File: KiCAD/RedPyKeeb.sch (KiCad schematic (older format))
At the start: 4 parts, among them J0 Conn_01x04_MountingPin_PicoUSB, U0 USB_Pico, U1,0 Board_main_Pico, U1,1 Board_side_Pico

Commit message: Update KiCAD files
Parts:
- removed J0: Conn_01x04_MountingPin_PicoUSB, symbol Connector_Generic_MountingPin:Conn_01x04_MountingPin
- removed U1,0: Board_main_Pico, MCU_RaspberryPi_and_Boards:RPi_Pico_SMD_TH, symbol MCU_RaspberryPi_and_Boards:Pico
- removed U1,1: Board_side_Pico, MCU_RaspberryPi_and_Boards:RPi_Pico_SMD_TH, symbol MCU_RaspberryPi_and_Boards:Pico
- added J0, J1: Conn_01x04, Connector_JST:JST_EH_S4B-EH_1x04_P2.50mm_Horizontal, symbol Connector_Generic:Conn_01x04
- added U1, U2, U3: MCP23017_SO, Package_SO:SOIC-28W_7.5x17.9mm_P1.27mm, symbol Interface_Expansion:MCP23017_SO
- U0: footprint RPi_Pico:RPi_Pico_SMD_TH -> MCU_RaspberryPi_and_Boards:RPi_Pico_SMD_TH
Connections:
- net labels added: GNDPWR, IO_INT0, IO_INT1, IO_INT2, IO_INT3, LED_SCL_ROW0, LED_SCL_ROW1, LED_SCL_ROW2, LED_SCL_ROW3, LED_SCL_ROW4, LED_SCL_ROW5, LED_SCL_ROW6, LED_SDA_ROW0, LED_SDA_ROW1, LED_SDA_ROW2, LED_SDA_ROW3, LED_SDA_ROW4, LED_SDA_ROW5, LED_SDA_ROW6, MAIN_VBUS, USB_DN, USB_DP
- net labels removed: I2C_SCL1, I2C_SDA1, KEY_ROW0,1, KEY_ROW1,1, KEY_ROW2,1, KEY_ROW3,1, KEY_ROW4,1, KEY_ROW5,1, PICO_PWR
- wire segments 4 -> 0
- no-connect marks 82 -> 42
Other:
- note added: "LED IO controller"
- note added: "Use I2C for interboard comms.\nSDA0 on GPIO0\nSCL0 on GPIO1"
- note removed: "This needs a footprint that will allow me to solder a small 4 pin connector to connect to the C3 daughterboard that will screw into the case."
- note removed: "Use I2C for interboard comms.\nSDA0 on GPIO0\nSCL0 on GPIO1\nSDA1 on GPIO4\nSCL1 on GPIO5"
- moved on the sheet: U0

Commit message: Update KiCAD files
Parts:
- added C1, C2, C3: 0805B104K100CT, Capacitors_SMD:C_0805_HandSoldering, symbol Device:CP
- U0: footprint MCU_RaspberryPi_and_Boards:RPi_Pico_SMD_TH -> Custom_pico:RPi_Pico_SMD_TH; symbol MCU_RaspberryPi_and_Boards:Pico -> RPI_Pico:Pico
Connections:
- net GNDPWR: now also U0.44 (TP1), C1.2, C2.2, C3.2; no longer U0.38 (GND)
- net MAIN_VBUS: now also C1.1, C2.1, C3.1
- net USB_DN: now also U0.45 (TP2)
- net USB_DP: now also U0.46 (TP3)
- no-connect marks 42 -> 43
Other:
- note added: "0805B104K100CT for capacitors\n100nF"
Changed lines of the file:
@@
 $EndDescr
 $Sheet
-S 9650 750  500  300
+S 9150 750  500  300
 U 604A5E2C
 F0 "key_matrix" 39
@@
 Text Notes 2350 800  0    59   ~ 0
 TODO: Power bus needs to be sorted, see Unified-Daughterboard?\n
-Text Notes 11150 1350 2    59   ~ 0
+Text Notes 10650 1350 2    59   ~ 0
 KEY_* originates from this sheet
-$Comp
-L MCU_RaspberryPi_and_Boards:Pico U0
-U 1 1 62848745
-P 1900 3000
-F 0 "U0" H 1900 4215 50  0000 C CNN
-F 1 "USB_Pico" H 1900 4124 50  0000 C CNN
-F 2 "MCU_RaspberryPi_and_Boards:RPi_Pico_SMD_TH" V 1900 3000 50  0001 C CNN
-F 3 "" H 1900 3000 50  0001 C CNN
-	1    1900 3000
-	1    0    0    -1
-$EndComp
 Text GLabel 1200 2050 0    39   BiDi ~ 0
 I2C_SDA0
@@
 Text GLabel 7150 2350 2    39   BiDi ~ 0
 KEY_COL14
-Text GLabel 4200 2050 2    39   BiDi ~ 0
-MAIN_VBUS
-$Comp
-L power:GNDPWR #PWR0101
-U 1 1 633BF01D
-P 2600 2250
-F 0 "#PWR0101" H 2600 2050 50  0001 C CNN
-F 1 "GNDPWR" V 2605 2142 50  0000 R CNN
-F 2 "" H 2600 2200 50  0001 C CNN
-F 3 "" H 2600 2200 50  0001 C CNN
-	1    2600 2250
-	0    -1   -1   0
-$EndComp
+Text GLabel 3750 1800 0    39   BiDi ~ 0
+MAIN_VBUS
 $Comp
 L power:GNDPWR #PWR0102
@@
 	0    -1   -1   0
 $EndComp
-Text GLabel 6450 2050 2    39   BiDi ~ 0
-MAIN_VBUS
 Text GLabel 5750 2350 0    39   BiDi ~ 0
 I2C_SDA0
@@
 	0    -1   -1   0
 $EndComp
-Text GLabel 8800 2050 2    39   BiDi ~ 0
-MAIN_VBUS
 Text Notes 9100 1850 2    39   ~ 0
 LED IO controller
@@
 $EndComp
 $Comp
-L power:GNDPWR #PWR?
+L power:GNDPWR #PWR0101
 U 1 1 6434583E
 P 5200 1250
-F 0 "#PWR?" H 5200 1050 50  0001 C CNN
+F 0 "#PWR0101" H 5200 1050 50  0001 C CNN
 F 1 "GNDPWR" V 5205 1142 50  0000 R CNN
 F 2 "" H 5200 1200 50  0001 C CNN
@@
 $EndComp
 $Comp
-L power:GNDPWR #PWR?
+L power:GNDPWR #PWR0104
 U 1 1 64901E61
 P 3500 3950
-F 0 "#PWR?" H 3500 3750 50  0001 C CNN
+F 0 "#PWR0104" H 3500 3750 50  0001 C CNN
 F 1 "GNDPWR" V 3504 3841 50  0000 R CNN
 F 2 "" H 3500 3900 50  0001 C CNN
@@
 $EndComp
 $Comp
-L power:GNDPWR #PWR?
+L power:GNDPWR #PWR0106
 U 1 1 64903402
 P 3500 3850
-F 0 "#PWR?" H 3500 3650 50  0001 C CNN
+F 0 "#PWR0106" H 3500 3650 50  0001 C CNN
 F 1 "GNDPWR" V 3504 3741 50  0000 R CNN
 F 2 "" H 3500 3800 50  0001 C CNN
@@
 $EndComp
 $Comp
-L power:GNDPWR #PWR?
+L power:GNDPWR #PWR0107
 U 1 1 649035CF
 P 3500 3750
-F 0 "#PWR?" H 3500 3550 50  0001 C CNN
+F 0 "#PWR0107" H 3500 3550 50  0001 C CNN
 F 1 "GNDPWR" V 3504 3641 50  0000 R CNN
 F 2 "" H 3500 3700 50  0001 C CNN
@@
 $EndComp
 $Comp
-L power:GNDPWR #PWR?
+L power:GNDPWR #PWR0108
 U 1 1 649043C1
 P 5750 3850
-F 0 "#PWR?" H 5750 3650 50  0001 C CNN
+F 0 "#PWR0108" H 5750 3650 50  0001 C CNN
 F 1 "GNDPWR" V 5754 3741 50  0000 R CNN
 F 2 "" H 5750 3800 50  0001 C CNN
@@
 $EndComp
 $Comp
-L power:GNDPWR #PWR?
+L power:GNDPWR #PWR0109
 U 1 1 64904490
 P 5750 3750
-F 0 "#PWR?" H 5750 3550 50  0001 C CNN
+F 0 "#PWR0109" H 5750 3550 50  0001 C CNN
 F 1 "GNDPWR" V 5754 3641 50  0000 R CNN
 F 2 "" H 5750 3700 50  0001 C CNN
@@
 $EndComp
 $Comp
-L power:GNDPWR #PWR?
+L power:GNDPWR #PWR0110
 U 1 1 64904A18
 P 8100 3750
-F 0 "#PWR?" H 8100 3550 50  0001 C CNN
+F 0 "#PWR0110" H 8100 3550 50  0001 C CNN
 F 1 "GNDPWR" V 8104 3641 50  0000 R CNN
 F 2 "" H 8100 3700 50  0001 C CNN
@@
 Text GLabel 6250 1450 2    39   BiDi ~ 0
 I2C_SCL0
+Text GLabel 2100 1850 1    39   BiDi ~ 0
+USB_DN
+Text GLabel 2200 1850 1    39   BiDi ~ 0
+USB_DP
+$Comp
+L power:GNDPWR #PWR0111
+U 1 1 64912107
+P 1600 1850
+F 0 "#PWR0111" H 1600 1650 50  0001 C CNN
+F 1 "GNDPWR" V 1605 1742 50  0000 R CNN
+F 2 "" H 1600 1800 50  0001 C CNN
+F 3 "" H 1600 1800 50  0001 C CNN
+	1    1600 1850
+	-1   0    0    1
+$EndComp
+$Comp
+L RPI_Pico:Pico U0
+U 1 1 62848745
+P 1900 3000
+F 0 "U0" H 1900 4215 50  0000 C CNN
+F 1 "USB_Pico" H 1900 4124 50  0000 C CNN
+F 2 "Custom_pico:RPi_Pico_SMD_TH" V 1900 3000 50  0001 C CNN
+F 3 "" H 1900 3000 50  0001 C CNN
+	1    1900 3000
+	1    0    0    -1
+$EndComp
+$Comp
+L Device:CP C1
+U 1 1 64942561
+P 4350 1950
+F 0 "C1" V 4605 1950 50  0000 C CNN
+F 1 "0805B104K100CT" V 4514 1950 50  0000 C CNN
+F 2 "Capacitors_SMD:C_0805_HandSoldering" H 4388 1800 50  0001 C CNN
+F 3 "~" H 4350 1950 50  0001 C CNN
+	1    4350 1950
+	0    -1   -1   0
+$EndComp
+$Comp
+L Device:CP C2
+U 1 1 6494E898
+P 6600 2000
+F 0 "C2" V 6855 2000 50  0000 C CNN
+F 1 "0805B104K100CT" V 6764 2000 50  0000 C CNN
+F 2 "Capacitors_SMD:C_0805_HandSoldering" H 6638 1850 50  0001 C CNN
+F 3 "~" H 6600 2000 50  0001 C CNN
+	1    6600 2000
+	0    -1   -1   0
+$EndComp
+$Comp
+L Device:CP C3
+U 1 1 6494F130
+P 8950 2000
+F 0 "C3" V 9205 2000 50  0000 C CNN
+F 1 "0805B104K100CT" V 9114 2000 50  0000 C CNN
+F 2 "Capacitors_SMD:C_0805_HandSoldering" H 8988 1850 50  0001 C CNN
+F 3 "~" H 8950 2000 50  0001 C CNN
+	1    8950 2000
+	0    -1   -1   0
+$EndComp
+$Comp
+L power:GNDPWR #PWR0112
+U 1 1 64950902
+P 4500 1950
+F 0 "#PWR0112" H 4500 1750 50  0001 C CNN
+F 1 "GNDPWR" V 4505 1842 50  0000 R CNN
+F 2 "" H 4500 1900 50  0001 C CNN
+F 3 "" H 4500 1900 50  0001 C CNN
+	1    4500 1950
+	0    -1   -1   0
+$EndComp
+$Comp
+L power:GNDPWR #PWR0113
+U 1 1 64952DDE
+P 6750 2000
+F 0 "#PWR0113" H 6750 1800 50  0001 C CNN
+F 1 "GNDPWR" H 6754 1846 50  0000 C CNN
+F 2 "" H 6750 1950 50  0001 C CNN
+F 3 "" H 6750 1950 50  0001 C CNN
+	1    6750 2000
+	0    -1   -1   0
+$EndComp
+$Comp
+L power:GNDPWR #PWR0114
+U 1 1 64954015
+P 9100 2000
+F 0 "#PWR0114" H 9100 1800 50  0001 C CNN
+F 1 "GNDPWR" H 9104 1846 50  0000 C CNN
+F 2 "" H 9100 1950 50  0001 C CNN
+F 3 "" H 9100 1950 50  0001 C CNN
+	1    9100 2000
+	0    -1   -1   0
+$EndComp
+Wire Wire Line
+	3750 1800 4200 1800
+Wire Wire Line
+	4200 1800 4200 1950
+Connection ~ 4200 1800
+Wire Wire Line
+	6450 2050 6450 2000
+Connection ~ 6450 1800
+Wire Wire Line
+	8800 2050 8800 2000
+Connection ~ 8800 2000
+Wire Wire Line
+	8800 2000 8800 1800
+Connection ~ 6450 2000
+Wire Wire Line
+	6450 2000 6450 1800
+Wire Wire Line
+	6450 1800 8800 1800
+Connection ~ 4200 1950
+Wire Wire Line
+	4200 1950 4200 2050
+Wire Wire Line
+	4200 1800 6450 1800
+NoConn ~ 2600 2250
+Text Notes 2650 1200 0    39   ~ 0
+0805B104K100CT for capacitors\n100nF
 $EndSCHEMATC

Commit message: Update KiCAD files and README
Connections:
- net LED_SDA_ROW7: now reaches U3.28 (GPA7)
- net LED_SCL_ROW7: now reaches U3.8 (GPB7)
- no-connect marks 43 -> 41
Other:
- note added: "TODO: Power bus needs to be sorted, see Unified-Daughterboard?\nLED row 7 is for status indicators"
- note removed: "TODO: Power bus needs to be sorted, see Unified-Daughterboard?\n"
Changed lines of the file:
@@
 Use I2C for interboard comms.\nSDA0 on GPIO0\nSCL0 on GPIO1
 Text Notes 2350 800  0    59   ~ 0
-TODO: Power bus needs to be sorted, see Unified-Daughterboard?\n
+TODO: Power bus needs to be sorted, see Unified-Daughterboard?\nLED row 7 is for status indicators
 Text Notes 10650 1350 2    59   ~ 0
 KEY_* originates from this sheet
@@
 NoConn ~ 8100 3050
 NoConn ~ 8100 2950
-NoConn ~ 9500 3950
-NoConn ~ 9500 3050
 NoConn ~ 4900 3950
 NoConn ~ 7150 3950
@@
 Text Notes 2650 1200 0    39   ~ 0
 0805B104K100CT for capacitors\n100nF
+Text GLabel 9500 3050 2    39   BiDi ~ 0
+LED_SCL_ROW7
+Text GLabel 9500 3950 2    39   BiDi ~ 0
+LED_SDA_ROW7
 $EndSCHEMATC

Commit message: Update KiCAD files
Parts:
- added U10: PCA9306D, Package_SO:SO-8_3.9x4.9mm_P1.27mm, symbol Interface:PCA9306D
- added U11: TXB0104D, Package_SO:SOIC-14_3.9x8.7mm_P1.27mm, symbol Logic_LevelTranslator:TXB0104D
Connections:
- net GNDPWR: now also U10.1 (GND), U11.7 (GND)
- net I2C_SCL0: now also U10.6 (SCL2); no longer U0.2 (GPIO1)
- net I2C_SDA0: now also U10.5 (SDA2); no longer U0.1 (GPIO0)
- net IO_INT0: now also U11.10 (B4); no longer U0.6 (GPIO4)
- net IO_INT1: now also U11.11 (B3); no longer U0.7 (GPIO5)
- net IO_INT2: now also U11.12 (B2); no longer U0.9 (GPIO6)
- net IO_INT3: now also U11.13 (B1); no longer U0.10 (GPIO7)
- net MAIN_VBUS: now also U10.7 (VREF2), U10.8 (EN), U11.14 (VCCB)
- net PICO_33_REF: now reaches U0.4 (GPIO2)
- net PICO_33_REF: now also U10.2 (VREF1), U11.1 (VCCA), U11.8 (OE)
- new net: U0.10 (GPIO7), U11.2 (A1)
- new net: U0.9 (GPIO6), U11.3 (A2)
- new net: U0.7 (GPIO5), U11.4 (A3)
- new net: U0.6 (GPIO4), U11.5 (A4)
- new net: U0.2 (GPIO1), U10.3 (SCL1)
- new net: U0.1 (GPIO0), U10.4 (SDA1)
- no-connect marks 41 -> 40
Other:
- moved on the sheet: C1, C2, C3, U0, U1, U2, U3

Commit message: Update KiCAD files
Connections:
- net I2C_SCL0: no longer J1.2 (Pin_2)
- net I2C_SDA0: no longer J1.1 (Pin_1)
- net PICO_SCL0: now reaches U0.2 (GPIO1), U10.3 (SCL1)
- net PICO_SCL0: now also J1.2 (Pin_2)
- net PICO_SDA0: now reaches U0.1 (GPIO0), U10.4 (SDA1)
- net PICO_SDA0: now also J1.1 (Pin_1)
- no-connect marks 40 -> 41
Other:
- note added: "TODO: Power bus needs to be sorted, see Unified-Daughterboard?\n\nMCP23017_SO needs to have the interrupt pins (INT*)\nconfigured as not open-drain as the TXB0104D can't handle open-drain"
- note removed: "TODO: Power bus needs to be sorted, see Unified-Daughterboard?\nLED row 7 is for status indicators"
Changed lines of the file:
@@
 Text Notes 1950 1050 2    59   ~ 0
 Use I2C for interboard comms.\nSDA0 on GPIO0\nSCL0 on GPIO1
-Text Notes 2350 800  0    59   ~ 0
-TODO: Power bus needs to be sorted, see Unified-Daughterboard?\nLED row 7 is for status indicators
+Text Notes 2150 950  0    59   ~ 0
+TODO: Power bus needs to be sorted, see Unified-Daughterboard?\n\nMCP23017_SO needs to have the interrupt pins (INT*)\nconfigured as not open-drain as the TXB0104D can't handle open-drain
 Text Notes 10650 1350 2    59   ~ 0
 KEY_* originates from this sheet
@@
 $EndComp
 Text GLabel 6250 1550 2    39   BiDi ~ 0
-I2C_SDA0
+PICO_SDA0
 Text GLabel 6250 1450 2    39   BiDi ~ 0
-I2C_SCL0
+PICO_SCL0
 Text GLabel 3500 2050 1    39   BiDi ~ 0
 USB_DN
@@
 $EndComp
 $Comp
-L power:GNDPWR #PWR?
+L power:GNDPWR #PWR0116
 U 1 1 605F480A
 P 1750 1550
-F 0 "#PWR?" H 1750 1350 50  0001 C CNN
+F 0 "#PWR0116" H 1750 1350 50  0001 C CNN
 F 1 "GNDPWR" V 1755 1442 50  0000 R CNN
 F 2 "" H 1750 1500 50  0001 C CNN
@@
 	2300 3150 2600 3150
 $Comp
-L power:GNDPWR #PWR?
+L power:GNDPWR #PWR0117
 U 1 1 60612AD1
 P 1700 2800
-F 0 "#PWR?" H 1700 2600 50  0001 C CNN
+F 0 "#PWR0117" H 1700 2600 50  0001 C CNN
 F 1 "GNDPWR" V 1705 2692 50  0000 R CNN
 F 2 "" H 1700 2750 50  0001 C CNN
@@
 Wire Wire Line
 	2100 3800 2300 3800
+NoConn ~ 2350 6000
+Text GLabel 2350 1950 1    39   Input ~ 0
+PICO_SDA0
+Text GLabel 2350 2050 3    39   Input ~ 0
+PICO_SCL0
 $EndSCHEMATC

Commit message: Update KiCAD files
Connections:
- net LED_SCL_ROW0: now also U3.22 (GPA1); no longer U3.1 (GPB0)
- net LED_SCL_ROW1: now also U3.24 (GPA3); no longer U3.2 (GPB1)
- net LED_SCL_ROW2: now also U3.26 (GPA5); no longer U3.3 (GPB2)
- net LED_SCL_ROW3: now also U3.28 (GPA7); no longer U3.4 (GPB3)
- net LED_SCL_ROW4: now also U3.2 (GPB1); no longer U3.5 (GPB4)
- net LED_SCL_ROW5: now also U3.4 (GPB3); no longer U3.6 (GPB5)
- net LED_SCL_ROW6: now also U3.6 (GPB5); no longer U3.7 (GPB6)
- net LED_SDA_ROW1: now also U3.23 (GPA2); no longer U3.22 (GPA1)
- net LED_SDA_ROW2: now also U3.25 (GPA4); no longer U3.23 (GPA2)
- net LED_SDA_ROW3: now also U3.27 (GPA6); no longer U3.24 (GPA3)
- net LED_SDA_ROW4: now also U3.1 (GPB0); no longer U3.25 (GPA4)
- net LED_SDA_ROW5: now also U3.3 (GPB2); no longer U3.26 (GPA5)
- net LED_SDA_ROW6: now also U3.5 (GPB4); no longer U3.27 (GPA6)
- net LED_SDA_ROW7: now also U3.7 (GPB6); no longer U3.28 (GPA7)
- net KEY_COL20: now reaches U2.7 (GPB6)
- no-connect marks 41 -> 38
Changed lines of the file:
@@
 F1 "led_strings.sch" 39
 $EndSheet
-Text GLabel 6950 5900 2    39   BiDi ~ 0
+Text GLabel 6950 5800 2    39   BiDi ~ 0
 LED_SCL_ROW6
-Text GLabel 6950 5800 2    39   BiDi ~ 0
+Text GLabel 6950 5600 2    39   BiDi ~ 0
 LED_SCL_ROW5
+Text GLabel 6950 5400 2    39   BiDi ~ 0
+LED_SCL_ROW4
+Text GLabel 6950 6900 2    39   BiDi ~ 0
+LED_SCL_ROW3
+Text GLabel 6950 6700 2    39   BiDi ~ 0
+LED_SCL_ROW2
+Text GLabel 6950 6500 2    39   BiDi ~ 0
+LED_SCL_ROW1
+Text GLabel 6950 6300 2    39   BiDi ~ 0
+LED_SCL_ROW0
 Text GLabel 6950 5700 2    39   BiDi ~ 0
-LED_SCL_ROW4
-Text GLabel 6950 5600 2    39   BiDi ~ 0
-LED_SCL_ROW3
+LED_SDA_ROW6
 Text GLabel 6950 5500 2    39   BiDi ~ 0
-LED_SCL_ROW2
-Text GLabel 6950 5400 2    39   BiDi ~ 0
-LED_SCL_ROW1
+LED_SDA_ROW5
 Text GLabel 6950 5300 2    39   BiDi ~ 0
-LED_SCL_ROW0
+LED_SDA_ROW4
 Text GLabel 6950 6800 2    39   BiDi ~ 0
-LED_SDA_ROW6
-Text GLabel 6950 6700 2    39   BiDi ~ 0
-LED_SDA_ROW5
+LED_SDA_ROW3
 Text GLabel 6950 6600 2    39   BiDi ~ 0
-LED_SDA_ROW4
-Text GLabel 6950 6500 2    39   BiDi ~ 0
-LED_SDA_ROW3
+LED_SDA_ROW2
 Text GLabel 6950 6400 2    39   BiDi ~ 0
-LED_SDA_ROW2
-Text GLabel 6950 6300 2    39   BiDi ~ 0
 LED_SDA_ROW1
 Text GLabel 6950 6200 2    39   BiDi ~ 0
@@
 NoConn ~ 5550 5900
 NoConn ~ 2350 6900
-NoConn ~ 4600 6900
-NoConn ~ 4600 6000
-NoConn ~ 4600 5900
 Text GLabel 950  5900 0    39   BiDi ~ 0
 IO_INT0
@@
 Text GLabel 6950 6000 2    39   BiDi ~ 0
 LED_SCL_ROW7
-Text GLabel 6950 6900 2    39   BiDi ~ 0
+Text GLabel 6950 5900 2    39   BiDi ~ 0
 LED_SDA_ROW7
 Text GLabel 1350 2050 0    39   BiDi ~ 0
@@
 Text GLabel 2350 2050 3    39   Input ~ 0
 PICO_SCL0
+Text GLabel 4600 5900 2    39   BiDi ~ 0
+KEY_COL20
 $EndSCHEMATC

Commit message: Update KiCAD files
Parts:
- U1, U2, U3: value MCP23017_SO -> MCP23017-E/SO
- U10: value PCA9306D -> PCA9306DP
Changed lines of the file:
@@
 NoConn ~ 3300 4350
 NoConn ~ 3400 4350
-Text GLabel 4000 2350 2    39   BiDi ~ 0
+Text GLabel 4000 2350 2    39   Input ~ 0
 MAIN_VBUS
 NoConn ~ 2600 2450
@@
 NoConn ~ 4000 3050
 NoConn ~ 4000 3150
-Text GLabel 4000 3250 2    39   BiDi ~ 0
+Text GLabel 4000 3250 2    39   Input ~ 0
 PICO_RUN
 NoConn ~ 4000 3350
@@
 Text GLabel 4600 5300 2    39   BiDi ~ 0
 KEY_COL14
-Text GLabel 1200 4750 0    39   BiDi ~ 0
+Text GLabel 1200 4750 0    39   Input ~ 0
 MAIN_VBUS
 $Comp
@@
 P 3900 6100
 F 0 "U2" H 3900 7381 50  0000 C CNN
-F 1 "MCP23017_SO" H 3900 7290 50  0000 C CNN
+F 1 "MCP23017-E/SO" H 3900 7290 50  0000 C CNN
 F 2 "Package_SO:SOIC-28W_7.5x17.9mm_P1.27mm" H 4100 5100 50  0001 L CNN
 F 3 "http://ww1.microchip.com/downloads/en/DeviceDoc/20001952C.pdf" H 4100 5000 50  0001 L CNN
@@
 P 6250 6100
 F 0 "U3" H 6250 7381 50  0000 C CNN
-F 1 "MCP23017_SO" H 6250 7290 50  0000 C CNN
+F 1 "MCP23017-E/SO" H 6250 7290 50  0000 C CNN
 F 2 "Package_SO:SOIC-28W_7.5x17.9mm_P1.27mm" H 6450 5100 50  0001 L CNN
 F 3 "http://ww1.microchip.com/downloads/en/DeviceDoc/20001952C.pdf" H 6450 5000 50  0001 L CNN
@@
 	0    -1   -1   0
 $EndComp
-Text GLabel 5200 1550 2    39   BiDi ~ 0
+Text GLabel 5200 1550 2    39   Output ~ 0
 MAIN_VBUS
 Text GLabel 5200 1350 2    39   BiDi ~ 0
@@
 P 1650 6100
 F 0 "U1" H 1650 7381 50  0000 C CNN
-F 1 "MCP23017_SO" H 1650 7290 50  0000 C CNN
+F 1 "MCP23017-E/SO" H 1650 7290 50  0000 C CNN
 F 2 "Package_SO:SOIC-28W_7.5x17.9mm_P1.27mm" H 1850 5100 50  0001 L CNN
 F 3 "http://ww1.microchip.com/downloads/en/DeviceDoc/20001952C.pdf" H 1850 5000 50  0001 L CNN
@@
 I2C_SCL0
 NoConn ~ 2600 2650
-Text GLabel 5550 6200 0    39   BiDi ~ 0
-MAIN_VBUS
-Text GLabel 3200 6200 0    39   BiDi ~ 0
-MAIN_VBUS
-Text GLabel 950  6200 0    39   BiDi ~ 0
+Text GLabel 5550 6200 0    39   Input ~ 0
+MAIN_VBUS
+Text GLabel 3200 6200 0    39   Input ~ 0
+MAIN_VBUS
+Text GLabel 950  6200 0    39   Input ~ 0
 MAIN_VBUS
 $Comp
@@
 P 1750 2050
 F 0 "U10" H 1750 1369 50  0000 C CNN
-F 1 "PCA9306D" H 1750 1460 50  0000 C CNN
+F 1 "PCA9306DP" H 1750 1460 50  0000 C CNN
 F 2 "Package_SO:SO-8_3.9x4.9mm_P1.27mm" H 1750 1600 50  0001 C CNN
 F 3 "https://www.nxp.com/docs/en/data-sheet/PCA9306.pdf" H 1450 2500 50  0001 C CNN
@@
 Wire Wire Line
 	2550 2350 2600 2350
-Text GLabel 1350 2550 0    39   BiDi ~ 0
+Text GLabel 1350 2550 0    39   Input ~ 0
 MAIN_VBUS
 Wire Wire Line
@@
 Text GLabel 2100 4000 2    20   Input ~ 0
 PICO_33_REF
-Text GLabel 1600 4200 0    39   BiDi ~ 0
+Text GLabel 1600 4200 0    39   Input ~ 0
 MAIN_VBUS
 $Comp
@@
 	2100 3800 2300 3800
 NoConn ~ 2350 6000
-Text GLabel 2350 1950 1    39   Input ~ 0
+Text GLabel 2350 1950 1    39   BiDi ~ 0
 PICO_SDA0
-Text GLabel 2350 2050 3    39   Input ~ 0
+Text GLabel 2350 2050 3    39   BiDi ~ 0
 PICO_SCL0
 Text GLabel 4600 5900 2    39   BiDi ~ 0

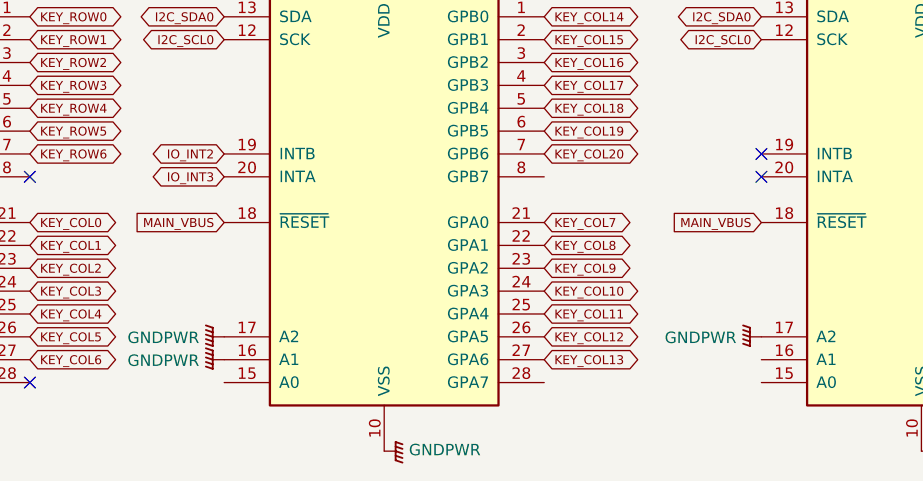
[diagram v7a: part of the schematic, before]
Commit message: Update KiCAD files to fix minor issues. Add initial release of firmware, not currently functioning.
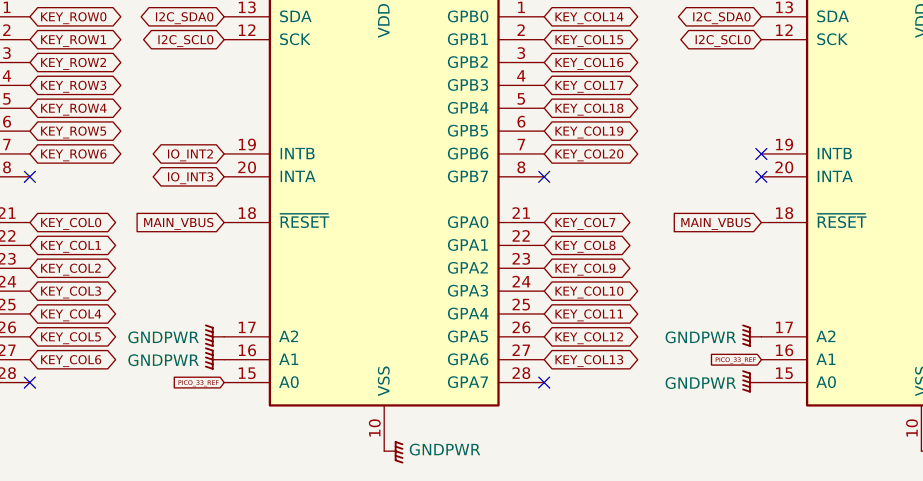
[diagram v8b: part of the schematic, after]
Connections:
- net GNDPWR: now also U3.15 (A0)
- net PICO_33_REF: now also U2.15 (A0), U3.16 (A1)
- no-connect marks 38 -> 40
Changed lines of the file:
@@
 Text GLabel 4600 5900 2    39   BiDi ~ 0
 KEY_COL20
+Text GLabel 3200 6900 0    20   Input ~ 0
+PICO_33_REF
+Text GLabel 5550 6800 0    20   Input ~ 0
+PICO_33_REF
+$Comp
+L power:GNDPWR #PWR?
+U 1 1 6056F226
+P 5550 6900
+F 0 "#PWR?" H 5550 6700 50  0001 C CNN
+F 1 "GNDPWR" V 5554 6791 50  0000 R CNN
+F 2 "" H 5550 6850 50  0001 C CNN
+F 3 "" H 5550 6850 50  0001 C CNN
+	1    5550 6900
+	0    1    1    0
+$EndComp
+NoConn ~ 4600 6900
+NoConn ~ 4600 6000
 $EndSCHEMATC
